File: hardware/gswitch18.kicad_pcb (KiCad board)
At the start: 2 copper layers, 48 x 32 mm, 26 parts, among them P1 JST GHS 1.25, P2 JST GHS 1.25, P3 JST GHS 1.25, P4 USB_B_Mini, P5 ISP, U1 ATMEGA88P, X1 12MHz

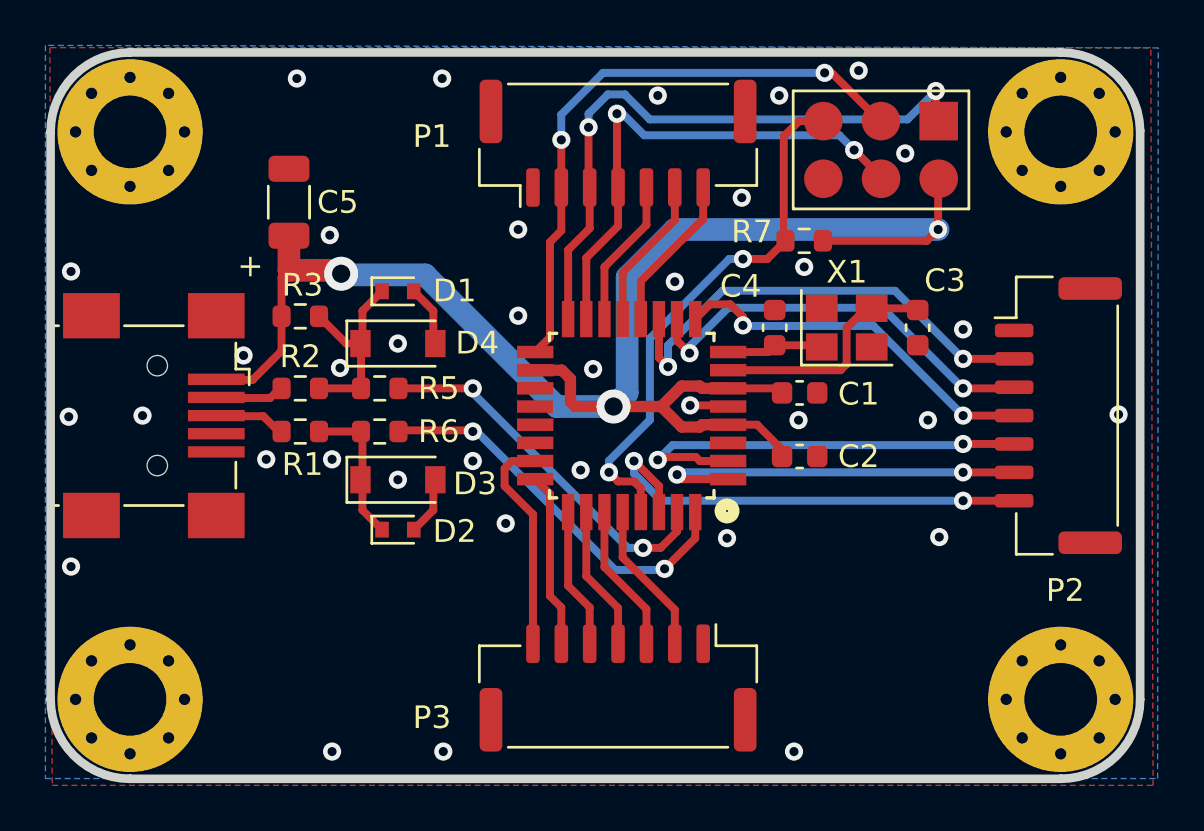
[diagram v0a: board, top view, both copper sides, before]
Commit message: PCB keepout under xtal & tweaks (version bumped to v1.2.1)
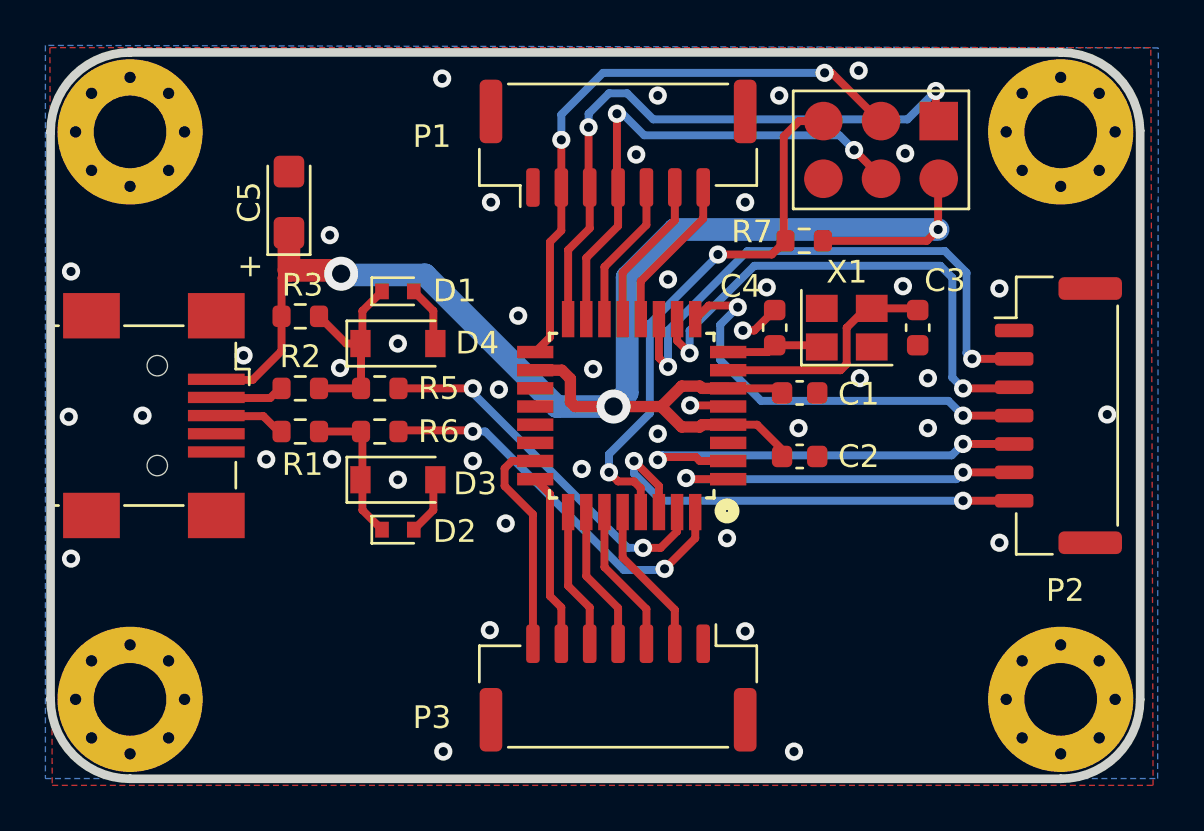
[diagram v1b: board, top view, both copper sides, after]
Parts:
- C5: footprint Capacitor_SMD:C_1206_3216Metric -> Capacitor_Tantalum_SMD:CP_EIA-3216-18_Kemet-A
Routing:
- net /SW08: track 18.5 -> 23.0 mm
- net /SW07: track 20.7 -> 24.7 mm
- net /SW09: track 16.6 -> 18.8 mm
- net GND: track 6.84 -> 8.61 mm, vias 36 -> 43
- net /SW11: track 17.2 -> 16.5 mm

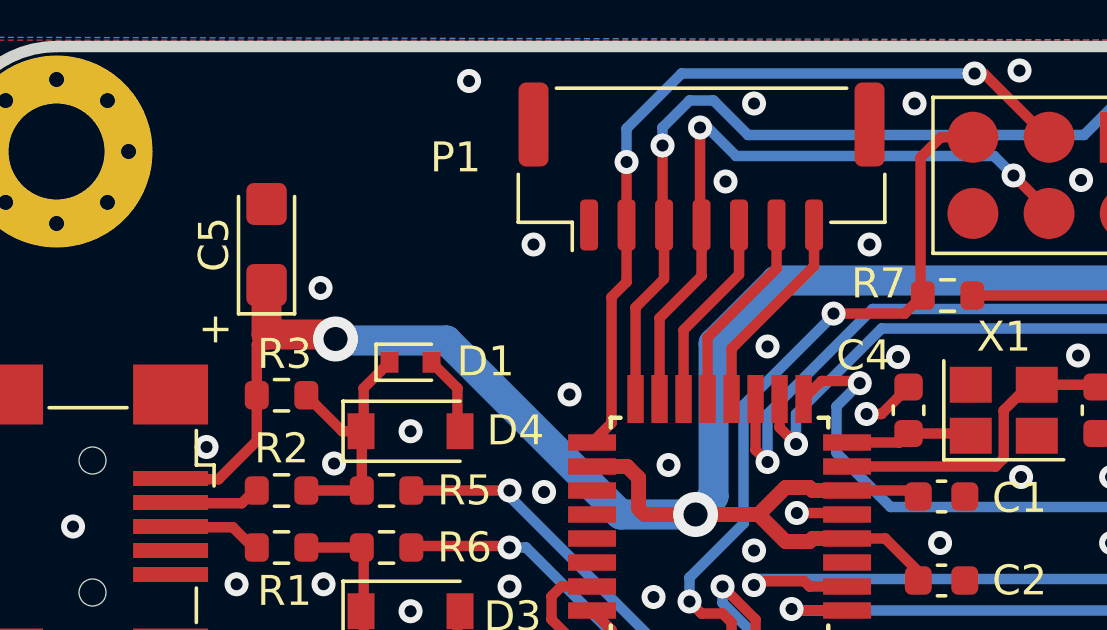
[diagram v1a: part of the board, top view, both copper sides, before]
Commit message: Schematic tidy-up (wasting time because why not?)
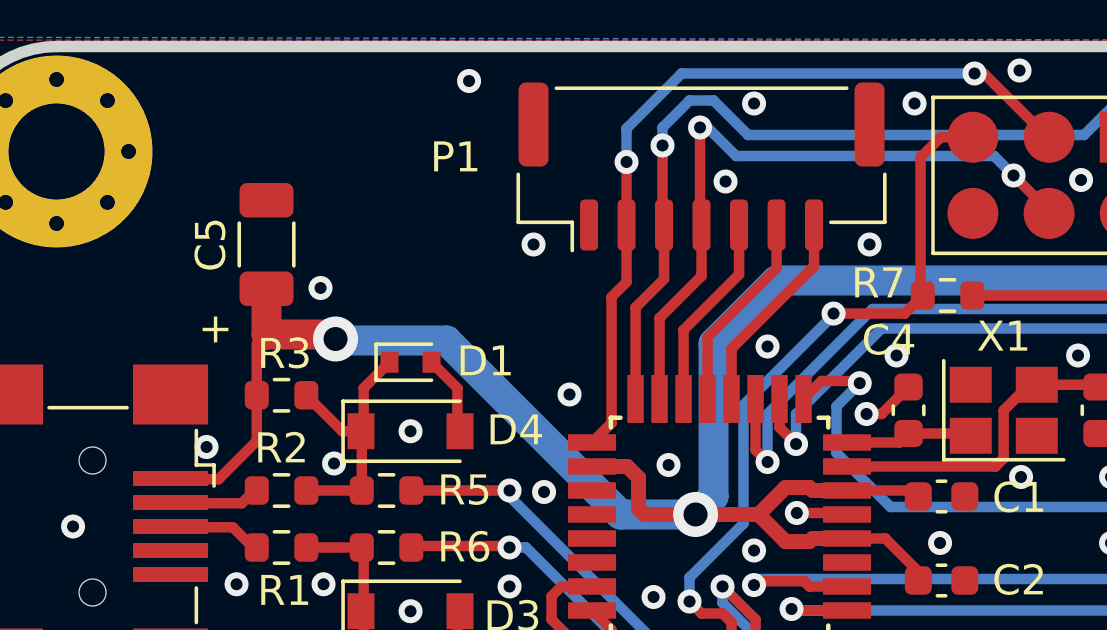
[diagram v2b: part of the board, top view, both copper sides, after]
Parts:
- C5: footprint Capacitor_Tantalum_SMD:CP_EIA-3216-18_Kemet-A -> Capacitor_SMD:C_1206_3216Metric
- turned C4 to -90 degrees
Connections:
- net /D+ renamed D+
- net /D- renamed D-
- net /MISO renamed SW02
- net /MOSI renamed SW03
- net /RESET renamed RESET
- net /SCK renamed SW01
- net /SW04 renamed SW04
- net /SW05 renamed SW05
- net /SW06 renamed SW06
- net /SW07 renamed SW07
- net /SW08 renamed SW08
- net /SW09 renamed SW09
- net /SW10 renamed SW10
- net /SW11 renamed SW11
- net /SW12 renamed SW12
- net /SW13 renamed SW13
- net /SW14 renamed SW14
- net /SW15 renamed SW15
- net /SW16 renamed SW16
- net /SW17 renamed SW17
- net /SW18 renamed SW18
- C4 pad 1: Net-(C4-Pad1) -> GND
- C4 pad 2: GND -> Net-(C4-Pad2)
- U1 pad 8: Net-(C4-Pad1) -> Net-(C4-Pad2)
- X1 pad 1: Net-(C4-Pad1) -> Net-(C4-Pad2)
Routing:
- net Net-(C4-Pad2): track 0.00 -> 4.28 mm
- net Net-(C4-Pad1): track 4.28 -> 0.00 mm
